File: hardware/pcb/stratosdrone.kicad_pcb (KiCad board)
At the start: 4 copper layers, 42 x 42 mm, 105 parts, among them J1 BATT_PH2, J10 DBG, J11 C6DBG, J2 USB-C-16P, J3 FLOW_HDR, J4 CAM_FFC15, J5 MOTOR1, J6 MOTOR2, J7 MOTOR3, J8 MOTOR4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

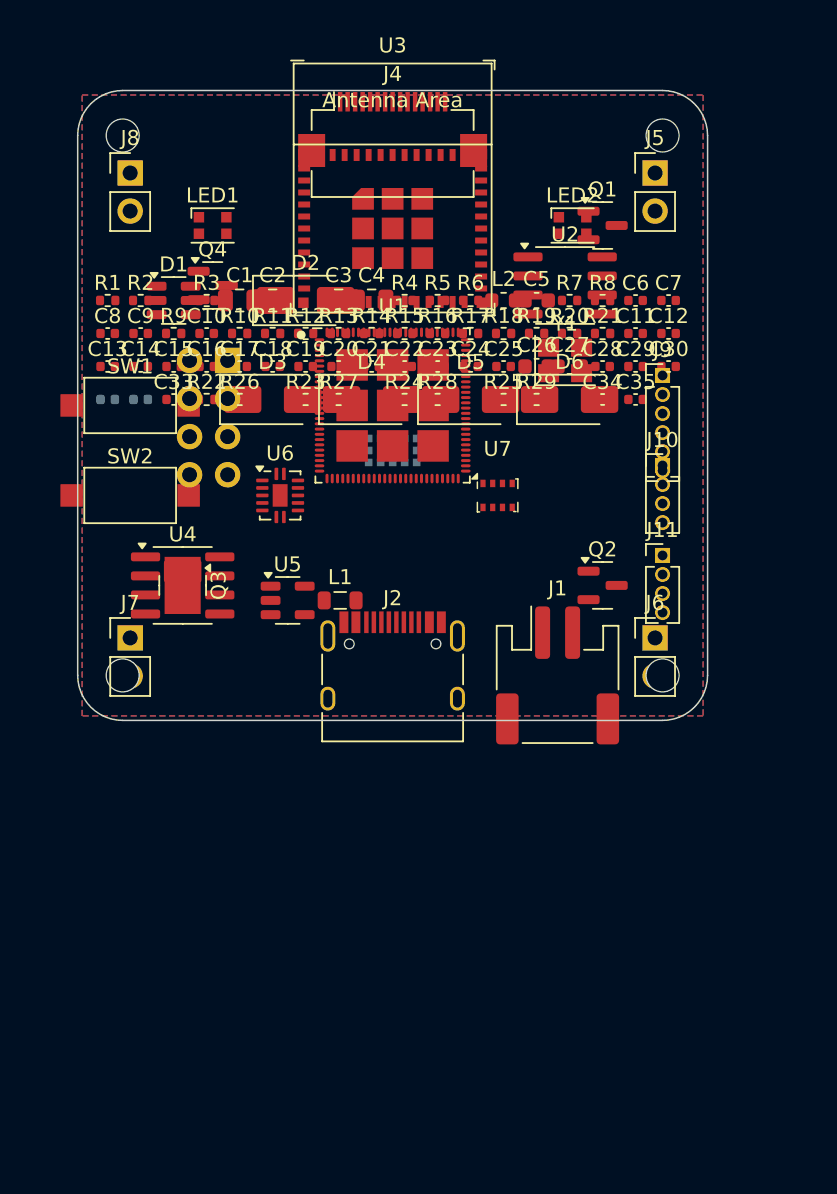
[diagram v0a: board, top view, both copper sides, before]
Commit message: Add Tello-style closed body + reshape PCB to Tello-style + component map
CAD: hardware/frame/tello_style/ — closed clamshell body in the DJI Tello
size class (98x92.5mm, 118mm wheelbase, 3in props) but distinct (hex motor
nacelles, faceted vented canopy, chamfered camera nose, slide-in rear
battery). body_bottom/body_top/assembly .scad + STL + previews. The open
X-frame stays as the alternative.

PCB: reshaped from 42x42 square to a 48x54 portrait Tello-style board that
fills the body pod — camera FFC at the nose, USB-C/battery at the rear,
motors at the four corners, M2 holes at 40x46 matching the pod bosses.
Rectangular mounting-hole support in gen_pcb; all 101 components re-placed;
consistency check still green; fab files regenerated.

Docs: gen_component_map.py renders an annotated top+bottom component map
(colour-coded by subsystem, every reference labelled + a table) into
preview/component_map.png, wired into 'make map' and shown in the READMEs.
CAD CI renders the new body and asserts its 118mm wheelbase.
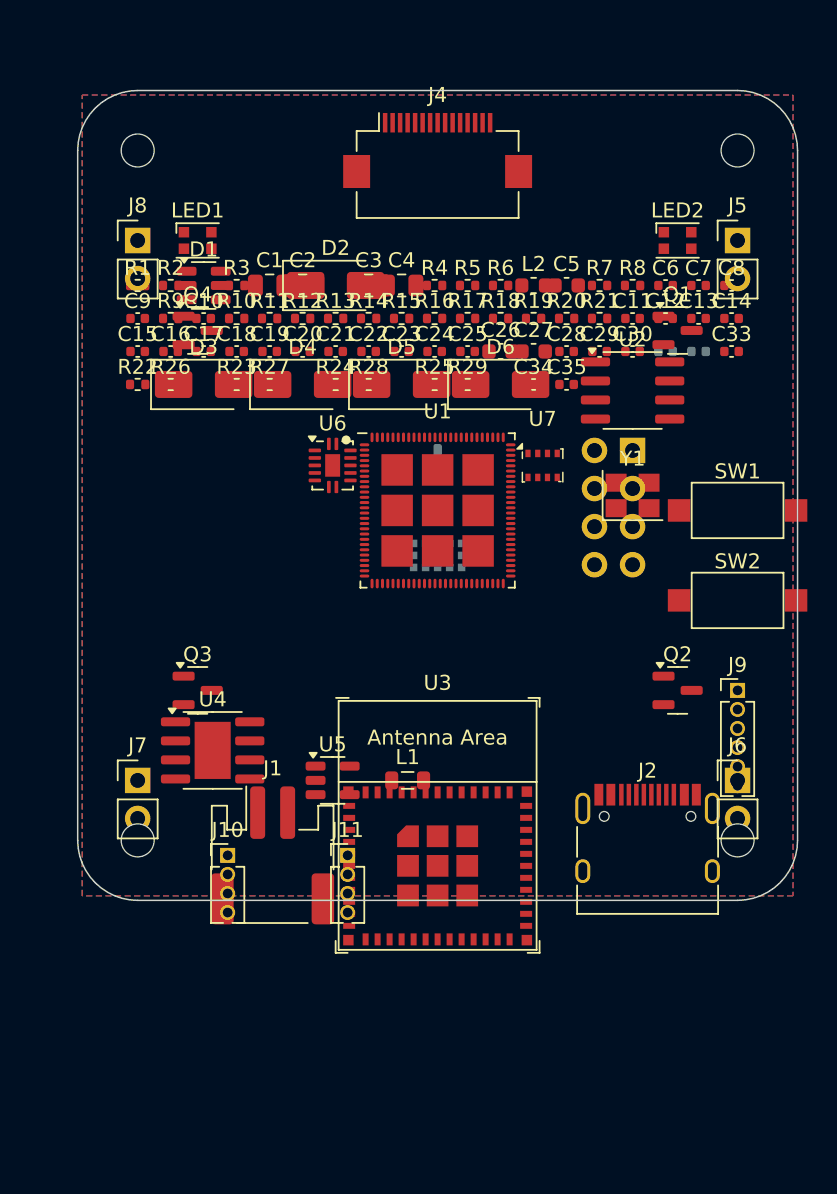
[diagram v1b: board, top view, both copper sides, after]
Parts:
- removed the ? at (3.00, 3.00)
- removed the ? at (39.0, 39.0)
- removed the ? at (3.00, 39.0)
- removed the ? at (39.0, 3.00)
- added ?: , , F.Cu at (4.00, 4.00)
- added ?: , , F.Cu at (44.0, 50.0)
- added ?: , , F.Cu at (44.0, 4.00)
- added ?: , , F.Cu at (4.00, 50.0)
- moved U3 42.6 mm to (24.0, 49.0)
- moved C8 41.7 mm to (43.6, 13.0)
- moved SW1 41.1 mm to (44.0, 28.0)
- moved SW2 41.1 mm to (44.0, 34.0)
- moved C13 39.5 mm to (41.4, 15.2)
- moved C14 39.5 mm to (43.6, 15.2)
- moved J10 38.9 mm to (10.0, 51.0)
- moved C31 37.3 mm to (39.2, 17.4)
- moved C33 37.3 mm to (43.6, 17.4)
- moved C32 37.3 mm to (41.4, 17.4)
- moved J11 29.0 mm to (18.0, 51.0)
- moved J3 27.7 mm to (37.0, 24.0)
- moved J1 22.5 mm to (13.0, 51.0)
- moved J9 21.6 mm to (44.0, 40.0)
- moved J2 20.5 mm to (38.0, 51.0)
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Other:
- board size 42 x 42 mm -> 48 x 54 mm

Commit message: Reshape to real-Tello-mainboard style: narrow portrait PCB + elongated body + sim
Following the reference Tello photos:

PCB: from 48x54 to a narrow PORTRAIT 32x66 mm board like the real Tello
mainboard — camera FFC at the nose, ESP32-C6 (RF) + ESP32-P4 (CPU) in
silkscreen shield zones down the spine, the two downward sensors on the
bottom, motor pads M1-M4 at the four corners, USB-C on the left side edge,
battery at the rear. Added Tello-style silkscreen (shield outlines, CAM/RF/
CPU section labels, FRONT arrow, motor marks). Passives flow to the rear so
the MCU/sensor spine stays readable. Consistency check still green; BOM/CPL/
gerbers and the annotated component map regenerated.

Body (frame/tello_style): elongated narrow pod (36x70) with slimmer arms to
match the new board and the real Tello silhouette; USB cutout moved to the
side wall; longer bottom sensor window covering both downward sensors;
bosses at the 24x58 pitch.

Sim: model.sdf visuals redone as an elongated narrow Tello body (camera bump
at the nose, rear battery, slim arms). Physical params (118 mm wheelbase,
92 g, inertia, motor coefficients) unchanged, so SITL/Gazebo flight is
identical — fc_core 3/3, SITL 5/5, Gazebo 2/2 still green.
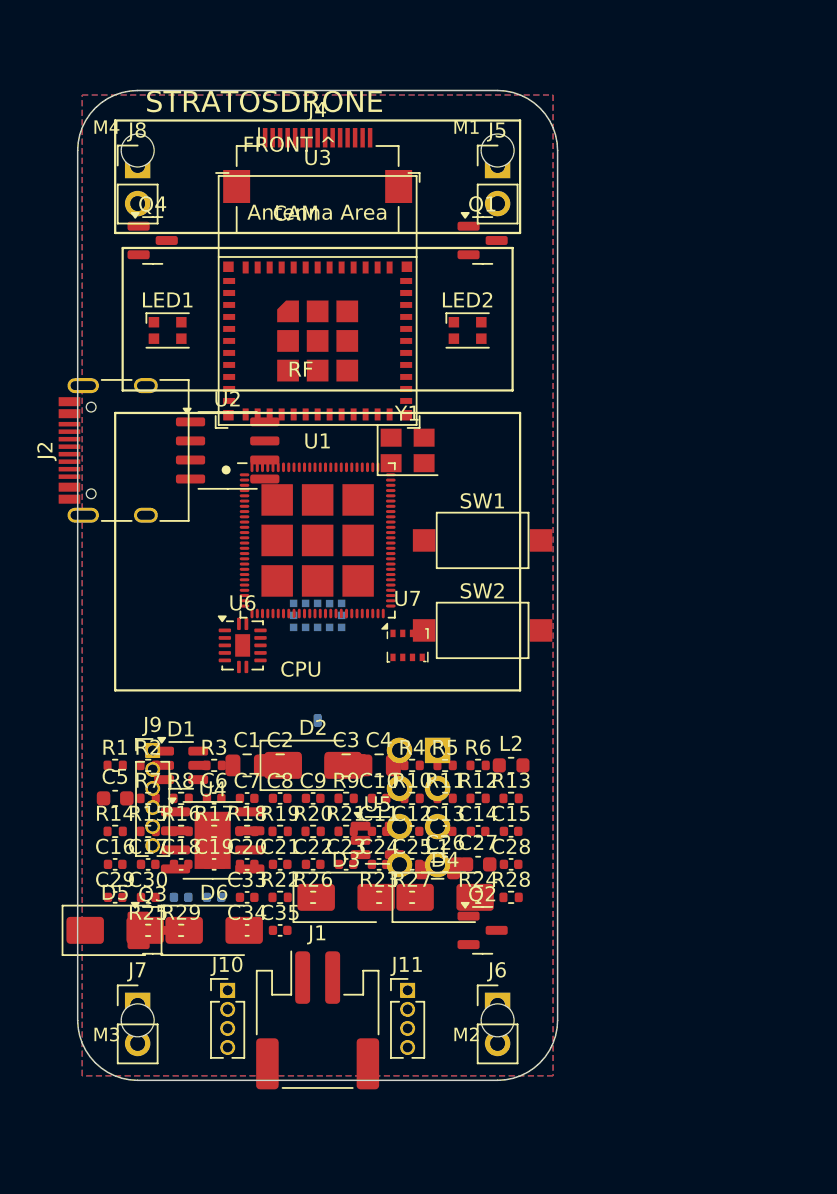
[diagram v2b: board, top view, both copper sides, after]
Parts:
- removed the ? at (44.0, 50.0)
- removed the ? at (44.0, 4.00)
- removed the ? at (4.00, 50.0)
- added ?: , , F.Cu at (28.0, 4.00)
- added ?: , , F.Cu at (28.0, 62.0)
- added ?: , , F.Cu at (4.00, 62.0)
- moved C31 48.7 mm to (6.90, 53.8)
- moved C29 48.7 mm to (2.50, 53.8)
- moved C30 48.7 mm to (4.70, 53.8)
- moved C32 48.7 mm to (9.10, 53.8)
- moved C33 48.7 mm to (11.3, 53.8)
- moved C6 45.6 mm to (9.10, 47.2)
- moved C7 45.6 mm to (11.3, 47.2)
- moved C8 45.6 mm to (13.5, 47.2)
- moved R7 45.6 mm to (4.70, 47.2)
- moved R8 45.6 mm to (6.90, 47.2)
- moved C5 45.6 mm to (2.50, 47.2)
- moved J2 43.8 mm to (3.50, 24.0), turned to 90 degrees
- moved C34 41.1 mm to (11.3, 56.0)
- moved C35 41.1 mm to (13.5, 56.0)
- moved D5 41.1 mm to (2.50, 56.0)
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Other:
- board size 48 x 54 mm -> 32 x 66 mm
- board text added: "CAM"
- board text added: "CPU"
- board text added: "FLOW + ToF"
- board text added: "FRONT ^"
- board text added: "M1"
- board text added: "M2"
- board text added: "M3"
- board text added: "M4"
- board text added: "RF"
- board text added: "STRATOSDRONE"

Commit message: PCB: real anchor-based placement (decoupling rings the P4) — zero overlaps
Replaced the naive auto-flow with a proper placer in gen_pcb.py:
- anchor_map(): each passive is associated with the part it serves, via its
  most-specific shared net (XTAL caps -> crystal, gate R/flyback -> their FET,
  flash pull-ups -> flash, ...) plus overrides for regulator/bulk/decoupling.
- collision-avoidance find_slot(): clusters each passive tight to its anchor
  via fine expanding rings, with a full-board grid fallback; mounting holes
  are registered as obstacles; a repair pass relocates any residual clash.
Result: decoupling caps ring the ESP32-P4, the power/charger parts cluster at
their regulators, motor parts sit at the four corners — verified 0 copper-pad
overlaps. The board is genuinely routable now.

Sized the board to 36x70 mm (still Tello portrait ~1:1.9) for routing room;
body pod -> 40x74, bosses 26x60; STL + previews + BOM/CPL/gerbers + component
map regenerated; consistency green. Updated KNOWN_GAPS (placement now done).
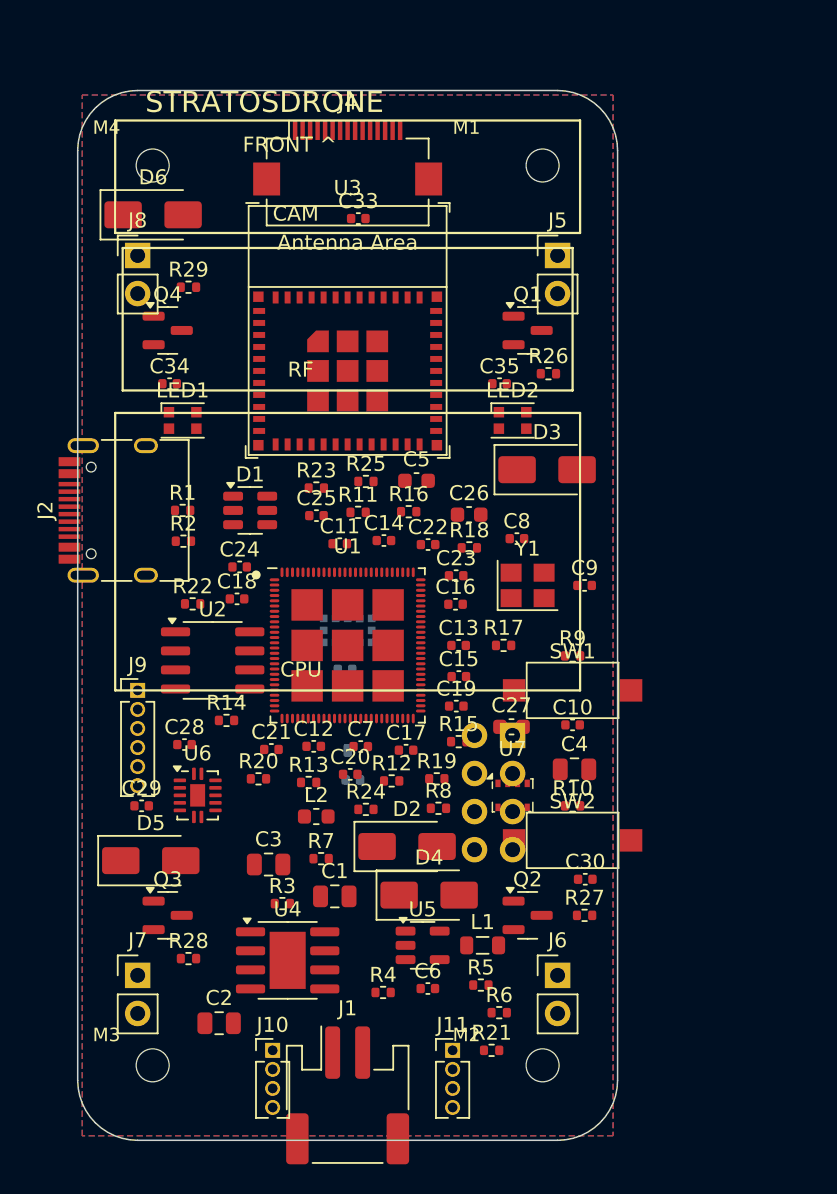
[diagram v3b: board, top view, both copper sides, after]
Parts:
- removed the ? at (28.0, 4.00)
- removed the ? at (28.0, 62.0)
- removed the ? at (4.00, 62.0)
- removed the ? at (4.00, 4.00)
- added ?: , , F.Cu at (31.0, 65.0)
- added ?: , , F.Cu at (5.00, 65.0)
- added ?: , , F.Cu at (5.00, 5.00)
- added ?: , , F.Cu at (31.0, 5.00)
- moved D6 47.9 mm to (5.03, 8.29)
- moved C33 45.9 mm to (18.7, 8.54)
- moved R29 42.9 mm to (7.39, 13.1)
- moved C35 39.3 mm to (28.1, 19.6)
- moved R26 38.3 mm to (31.4, 18.9)
- moved C34 36.8 mm to (6.13, 19.6)
- moved R25 33.3 mm to (19.2, 26.1)
- moved D3 31.5 mm to (31.3, 25.3)
- moved C5 29.2 mm to (22.6, 26.0)
- moved C30 29.2 mm to (33.8, 52.6)
- moved C16 28.6 mm to (25.2, 34.3)
- moved R23 27.6 mm to (15.9, 26.5)
- moved R16 26.2 mm to (22.1, 28.1)
- moved C25 24.1 mm to (15.9, 28.3)
- moved R18 24.0 mm to (26.1, 30.5)
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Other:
- board size 32 x 66 mm -> 36 x 70 mm

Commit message: pcb: fix VL53L1X (U8) — correct footprint + datasheet pinout
The ToF sensor was on the wrong footprint (OptoDevice:ST_VL53L0X) with a
pad map to match, leaving supply and I2C pins on the wrong pads. Moved U8 to
KiCad's official Sensor_Distance:ST_VL53L1x land and rewired pad-by-pad to the
ST VL53L1X datasheet:

  1 AVDDVCSEL=3V3   2 AVSSVCSEL=GND   3/4/6/12 GND   5 XSHUT
  7 GPIO1=INT       8 DNC (floating)  9 SDA  10 SCL  11 AVDD=3V3

Regenerated board + BOM/CPL; make check still passes. KNOWN_GAPS item 8 marks
U8 resolved (LCSC C2970716 rotation for the JLC CPL still to confirm).

First of the KNOWN_GAPS verification pass toward an orderable board.

https://claude.ai/code/session_011szEEHZ8KTTsZmGFgY6Cjw
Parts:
- U8: footprint ST_VL53L0X -> ST_VL53L1x
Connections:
- U8 pad 1: GND -> 3V3
- U8 pad 10: I2C_SDA -> I2C_SCL
- U8 pad 11: (no net) -> 3V3
- U8 pad 12: (no net) -> GND
- U8 pad 2: (no net) -> GND
- U8 pad 3: (no net) -> GND
- U8 pad 4: VL53_XSHUT -> GND
- U8 pad 5: 3V3 -> VL53_XSHUT
- U8 pad 6: 3V3 -> GND
- U8 pad 8: I2C_SCL -> (no net)
- U8 pad 9: (no net) -> I2C_SDA

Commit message: pcb: fix TP4056 (U4) charger pinout — STDBY/CE were miswired
Pin 6 (STDBY, open-collector status) was shorted straight to VBAT
instead of being wired as the status output, and pin 8 (CE, enable
input) was aliased to STDBY_N instead of being driven at all. Both
are real electrical bugs, not just unverified guesses.

Re-verified the full 8-pin + EP map against the Nanjing Top Power
TP4056-42-ESOP8 datasheet pin table and cross-checked against an
independent KiCad symbol: 1 TEMP, 2 PROG, 3 GND, 4 VCC, 5 BAT,
6 STDBY, 7 CHRG, 8 CE, EP=GND. Fixed pin 6 -> STDBY_N and pin 8 ->
VBUS (CE tied straight to VCC so charging is always enabled, since
this design has no software charge-enable line — the standard
reference circuit when no MCU control is needed).

Also confirmed R3=1.2k on PROG gives 1200/R(kOhm)=1.0A, an
appropriate ~0.9C rate for the 1S 1100mAh pack in the BOM, and that
grounding TEMP to disable the NTC is correct per datasheet.

Regenerated board/fab outputs via `make all`; consistency check
passes.
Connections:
- U4 pad 6: VBAT -> STDBY_N
- U4 pad 8: STDBY_N -> VBUS

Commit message: hardware/pcb: fix critical ICM-42688-P (U6) pinout — both power pins were grounded
The previous map tied VDDIO (real pin 5) and VDD (real pin 8) to GND, so the
IMU could never power up, and wired the host SPI signals to reserved/no-connect
pads instead of the chip's real AP_CS/AP_SCLK/AP_SDI pins (12/13/14).

Re-verified the full 14-pin LGA pinout against the TDK InvenSense DS-000347
pin table and an independent, manufacturer-tagged KiCad symbol, then rewired
every pad accordingly. Pad-level mapping confirmed via pcbnew after
regeneration.
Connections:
- U6 pad 1: CS_IMU -> SPI_MISO
- U6 pad 10: SPI_MISO -> GND
- U6 pad 11: 3V3 -> GND
- U6 pad 12: GND -> CS_IMU
- U6 pad 13: 3V3 -> SPI_SCLK
- U6 pad 14: GND -> SPI_MOSI
- U6 pad 15: (no net) -> GND
- U6 pad 2: SPI_SCLK -> GND
- U6 pad 3: SPI_MOSI -> GND
- U6 pad 4: GND -> IMU_INT
- U6 pad 5: GND -> 3V3
- U6 pad 8: GND -> 3V3
- U6 pad 9: IMU_INT -> GND

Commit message: hardware/pcb: fix critical SPL06-001 (U7) pinout — VDDIO grounded, SDA shorted
Same severity class as the U6 fix: the previous map tied real pin 6 (VDDIO)
to GND, hard-wired real pin 3 (SDA) straight to 3V3, and routed the host's
I2C_SDA net to real pin 1 (GND) -- shorting the shared I2C bus to ground
through this chip, which would have affected every other device on the bus.

Re-verified pad-by-pad against iNavFlight/hardware's SPL06 reference design,
which uses the identical official KiCad footprint. Pad-level mapping
confirmed via pcbnew after regeneration.
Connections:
- U7 pad 1: I2C_SDA -> GND
- U7 pad 3: 3V3 -> I2C_SDA
- U7 pad 6: GND -> 3V3

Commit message: hardware/pcb: verify SY8089 (U5) pinout, fix L1 inductor value mismatch
U5 SOT-23-5 pinout confirmed correct against the Silergy application note
(no change). L1 was labeled 2.2uH but its LCSC part (C408412) is actually a
10uH Sunlord MWSA0503S-100MT -- JLCPCB assembly stuffs the part the LCSC
code resolves to regardless of the printed value, so corrected the value
field to match reality. Also corrected a stale KNOWN_GAPS note: the FB
divider computes to 3.318V, not the previously-claimed 3.42V.
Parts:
- L1: value 2.2uH -> 10uH
